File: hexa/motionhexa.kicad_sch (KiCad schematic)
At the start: 2 parts, among them J1 Conn_01x13_Socket, J2 Conn_01x13_Socket

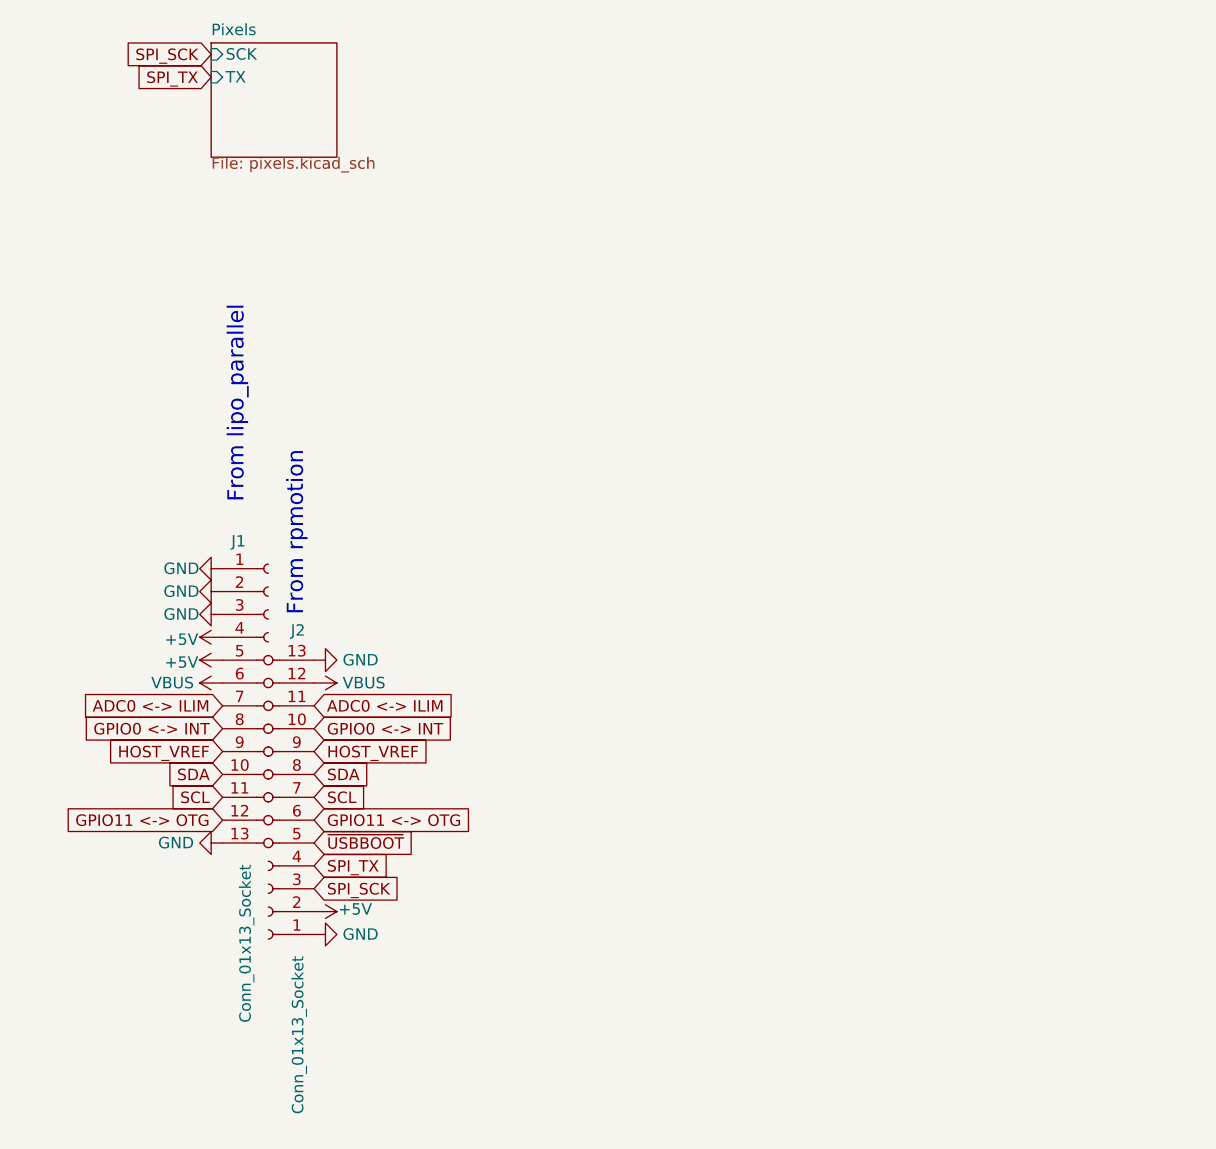
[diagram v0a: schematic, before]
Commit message: add mount points to motionhexa; add some silkscreen; fix DRC errors
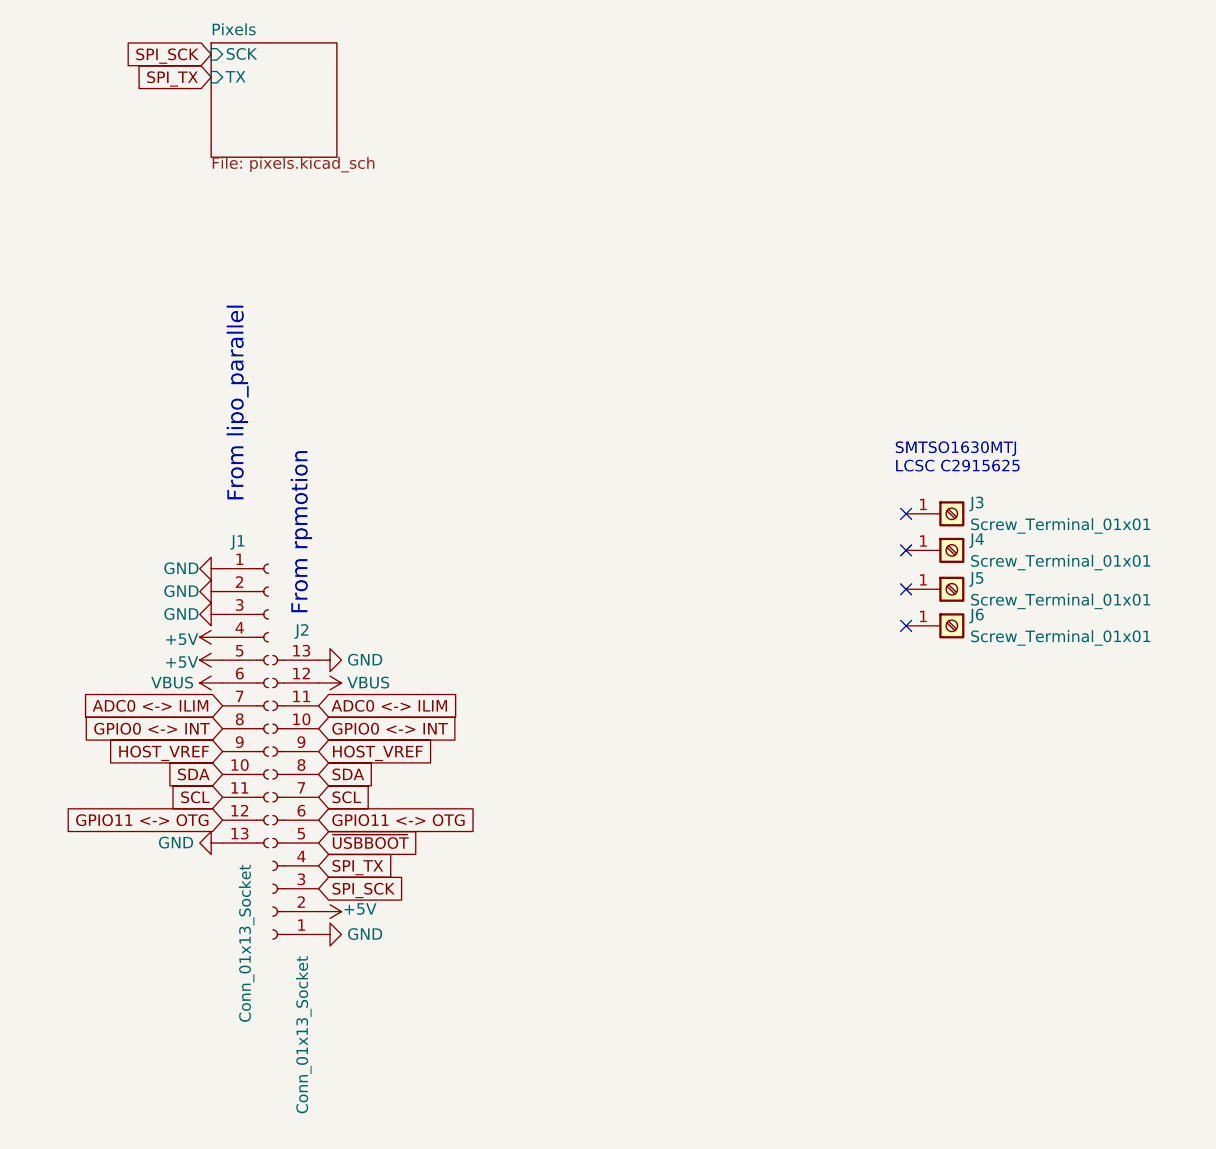
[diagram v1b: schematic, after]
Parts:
- added J3, J4, J5, J6: Screw_Terminal_01x01, motionhexa:SMTSO16, symbol Connector:Screw_Terminal_01x01
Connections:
- no-connect marks 0 -> 4
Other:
- note added: "SMTSO1630MTJ LCSC C2915625"
- moved on the sheet: J2

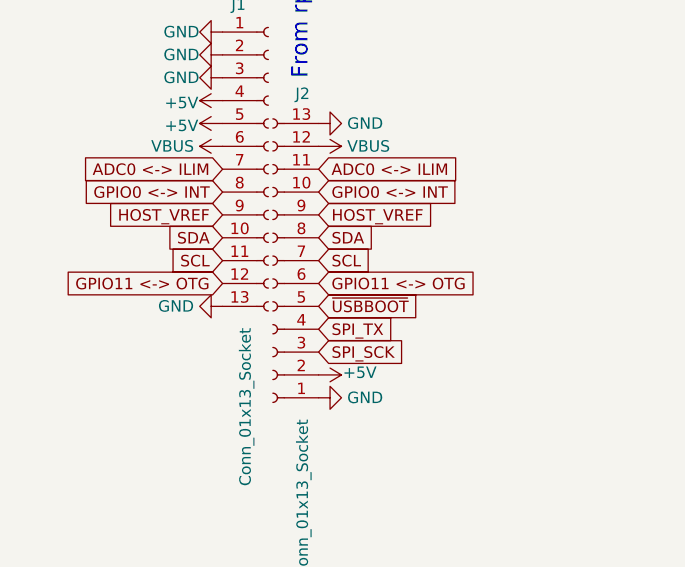
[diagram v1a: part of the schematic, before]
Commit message: power switch now controls OTG pin only, expectatio is that power consumption will be low enough with this PP; footprint for new power switch; updates to no longer export OTG pin; export SYS pin instead with no plan to use it
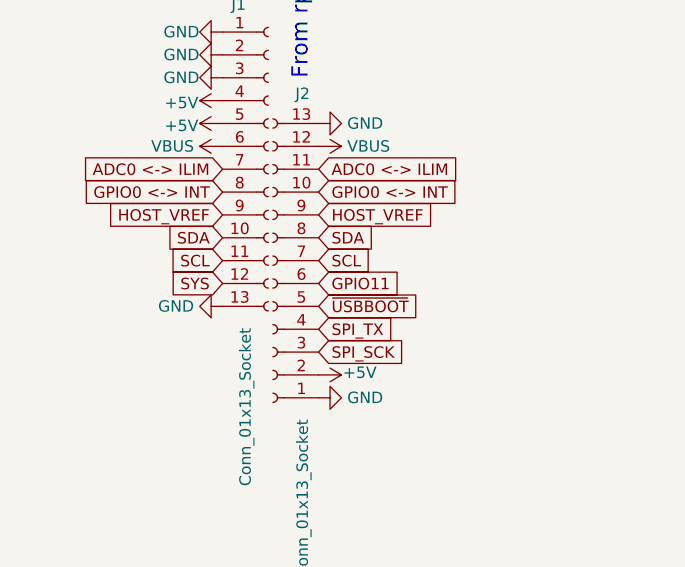
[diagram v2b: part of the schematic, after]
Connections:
- net GPIO11 <-> OTG renamed GPIO11
- net GPIO11: no longer J1.12 (Pin_12)
- new net SYS: J1.12 (Pin_12)
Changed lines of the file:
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@@
+    )
+  )
+  (global_label "SYS" (shape input) (at 106.68 110.49 180) (fields_autoplaced)
+    (effects (font (size 1.27 1.27)) (justify right))
+    (property "Intersheetrefs" "${INTERSHEET_REFS}" (at 100.1872 110.49 0)
+      (effects (font (size 1.27 1.27)) (justify right) hide)
     )
   )
@@
     )
   )
-  (global_label "GPIO11 <-> OTG" (shape input) (at 106.68 110.49 180) (fields_autoplaced)
-    (effects (font (size 1.27 1.27)) (justify right))
-    (property "Intersheetrefs" "${INTERSHEET_REFS}" (at 86.58 110.49 0)
-      (effects (font (size 1.27 1.27)) (justify right) hide)
-    )
-  )
   (global_label "SPI_SCK" (shape input) (at 117.348 118.11 0) (fields_autoplaced)
     (effects (font (size 1.27 1.27)) (justify left))
@@
     )
   )
-  (global_label "GPIO11 <-> OTG" (shape input) (at 117.348 110.49 0) (fields_autoplaced)
+  (global_label "GPIO11" (shape input) (at 117.348 110.49 0) (fields_autoplaced)
     (effects (font (size 1.27 1.27)) (justify left))
-    (property "Intersheetrefs" "${INTERSHEET_REFS}" (at 137.448 110.49 0)
+    (property "Intersheetrefs" "${INTERSHEET_REFS}" (at 127.2275 110.49 0)
       (effects (font (size 1.27 1.27)) (justify left) hide)
     )

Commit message: move attachment points farther out towards the edges so i can fit batteries in the space
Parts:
- J3, J4, J5, J6: now in the parts list
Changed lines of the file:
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@@
   )
   (symbol (lib_id "Connector:Screw_Terminal_01x01") (at 187.706 88.9 0) (unit 1)
-    (in_bom no) (on_board yes) (dnp no) (fields_autoplaced)
+    (in_bom yes) (on_board yes) (dnp no) (fields_autoplaced)
     (property "Reference" "J6" (at 189.738 87.6879 0)
       (effects (font (size 1.27 1.27)) (justify left))
@@
   )
   (symbol (lib_id "Connector:Screw_Terminal_01x01") (at 187.706 80.518 0) (unit 1)
-    (in_bom no) (on_board yes) (dnp no) (fields_autoplaced)
+    (in_bom yes) (on_board yes) (dnp no) (fields_autoplaced)
     (property "Reference" "J4" (at 189.738 79.3059 0)
       (effects (font (size 1.27 1.27)) (justify left))
@@
   )
   (symbol (lib_id "Connector:Screw_Terminal_01x01") (at 187.706 76.454 0) (unit 1)
-    (in_bom no) (on_board yes) (dnp no) (fields_autoplaced)
+    (in_bom yes) (on_board yes) (dnp no) (fields_autoplaced)
     (property "Reference" "J3" (at 189.738 75.2419 0)
       (effects (font (size 1.27 1.27)) (justify left))
@@
   )
   (symbol (lib_id "Connector:Screw_Terminal_01x01") (at 187.706 84.836 0) (unit 1)
-    (in_bom no) (on_board yes) (dnp no) (fields_autoplaced)
+    (in_bom yes) (on_board yes) (dnp no) (fields_autoplaced)
     (property "Reference" "J5" (at 189.738 83.6239 0)
       (effects (font (size 1.27 1.27)) (justify left))
